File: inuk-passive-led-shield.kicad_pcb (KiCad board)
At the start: 2 copper layers, 90 x 30 mm, 12 parts, among them J1 Conn_01x04_Male, J2 Conn_01x10_Male, J3 Conn_01x02_Male

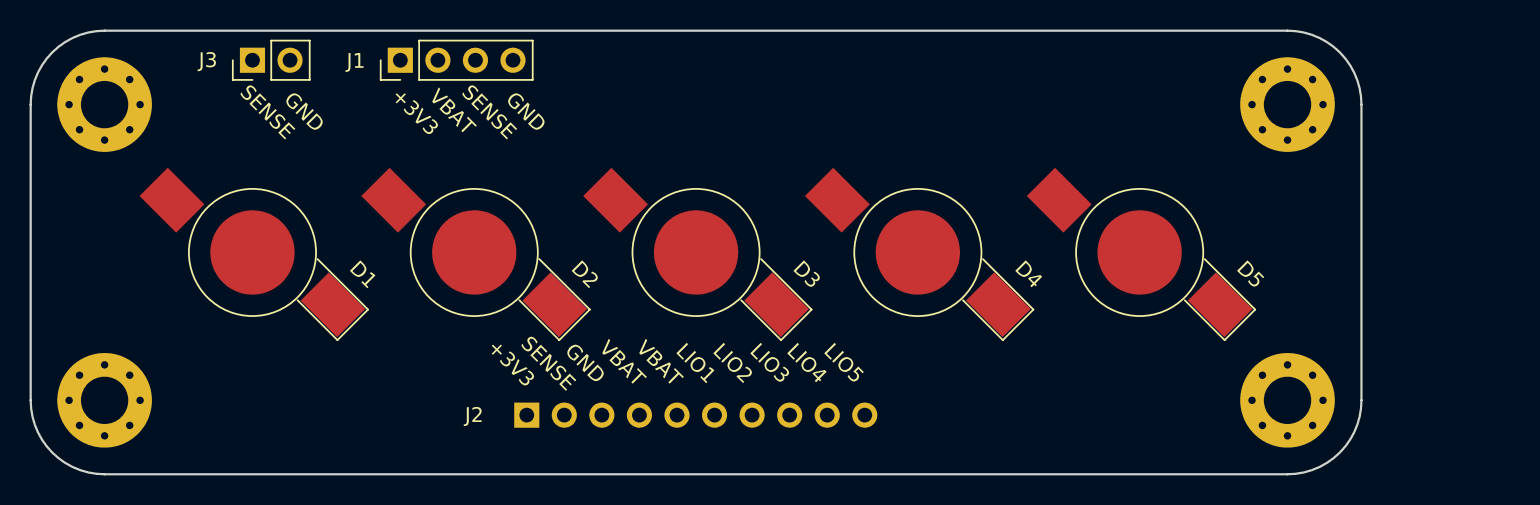
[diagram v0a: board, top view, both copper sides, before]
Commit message: added logo and info text for rev 0.9
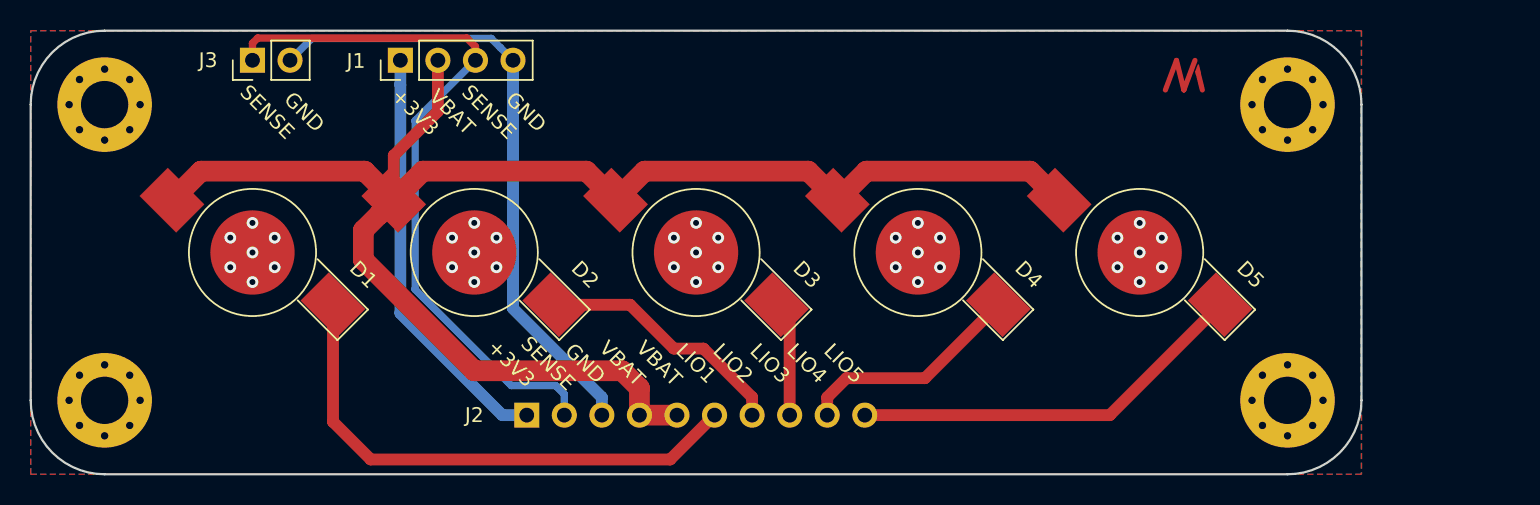
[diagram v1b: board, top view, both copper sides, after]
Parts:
- added U1: Logo_NM, Custom:Logo_NM, F.Cu at (133.0, 118.0)
- D1, D2, D3, D4, D5: value LED -> LED_PAD
- H1, H2, H3, H4: value MountingHole -> MountingHole_Pad
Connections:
- D1 pad 3: (no net) -> /thermal
- D2 pad 3: (no net) -> /thermal
- D3 pad 3: (no net) -> /thermal
- D4 pad 3: (no net) -> /thermal
- D5 pad 3: (no net) -> /thermal
- H1 pad 1: (no net) -> /thermal
- H2 pad 1: (no net) -> /thermal
- H3 pad 1: (no net) -> /thermal
- H4 pad 1: (no net) -> /thermal
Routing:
- net +BATT: track 0.00 -> 108.7 mm
- net /sense: track 0.00 -> 49.2 mm
- net GND: track 0.00 -> 42.8 mm
- net /lio1: track 0.00 -> 36.0 mm
- net +3V3: track 0.00 -> 28.5 mm
- net /lio5: track 0.00 -> 27.1 mm
- net /lio2: track 0.00 -> 17.1 mm
- net /lio4: track 0.00 -> 15.4 mm
- net /lio3: track 0.00 -> 7.83 mm
- net /thermal: vias 0 -> 35
- added copper zone on B.Cu, net /thermal
- added copper zone on F.Cu, net /thermal
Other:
- board text added: "Inuk passive led shield"
- board text added: "Rev: 0.9"

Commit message: resized board to 27 x 100 to fit on 100x100 panel
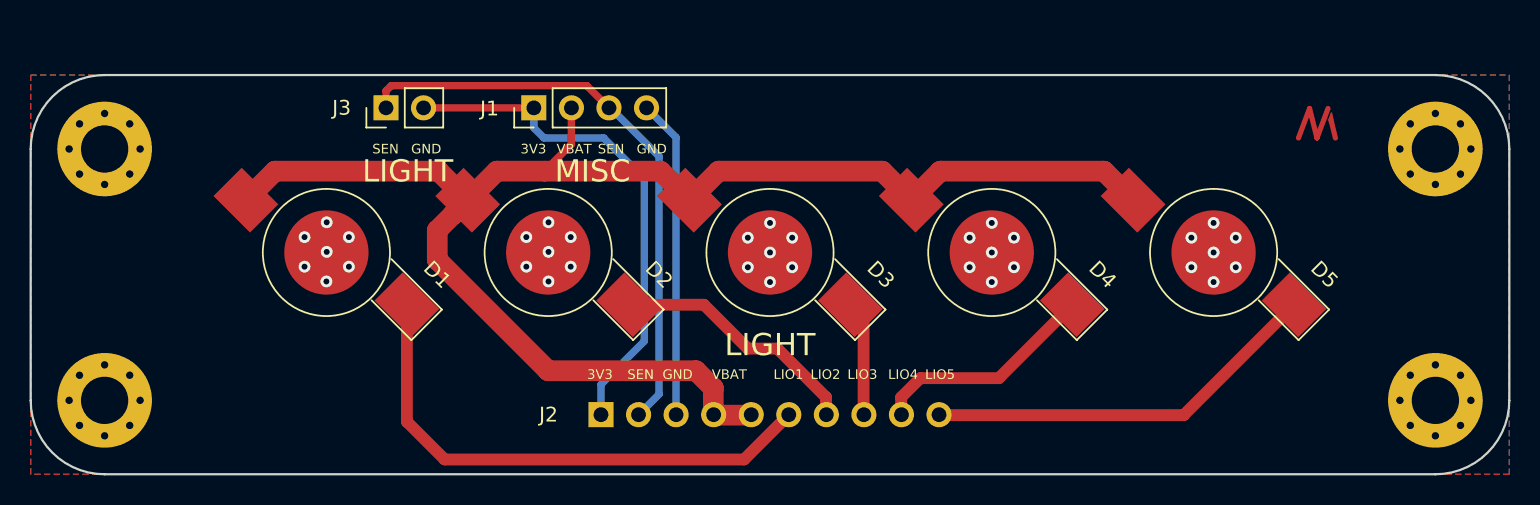
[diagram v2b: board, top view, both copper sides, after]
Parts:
- moved H2 10.4 mm to (150.0, 123.0)
- moved H3 10.0 mm to (150.0, 140.0)
- moved J1 9.59 mm to (89.0, 120.2)
- moved J3 9.59 mm to (79.0, 120.2)
- moved U1 9.57 mm to (142.0, 121.2)
- moved J2 5.02 mm to (93.6, 141.0)
- moved D1 5.00 mm to (75.0, 130.0)
- moved D2 5.00 mm to (90.0, 130.0)
- moved D3 5.00 mm to (105.0, 130.0)
- moved D4 5.00 mm to (120.0, 130.0)
- moved D5 5.00 mm to (135.0, 130.0)
- moved H1 3.00 mm to (60.0, 123.0)
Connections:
- J3 pad 2: GND -> +3V3
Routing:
- net GND: track 42.8 -> 21.6 mm
- net /sense: track 49.2 -> 39.8 mm
- net +3V3: track 28.5 -> 35.4 mm
- net +BATT: track 108.7 -> 103.1 mm
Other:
- board size 90 x 30 mm -> 100 x 27 mm
- board text added: "3V3"
- board text added: "LIGHT"
- board text added: "MISC"
- board text added: "SEN"
- board text removed: "+3V3"
- board text removed: "SENSE"

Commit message: created production files
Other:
- board text added: "Rev: 1.0"
- board text removed: "Rev: 0.9"
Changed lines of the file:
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@@
     (visible_elements FFFFFF7F)
     (pcbplotparams
-      (layerselection 0x00030_ffffffff)
+      (layerselection 0x010ff_ffffffff)
       (usegerberextensions false)
       (usegerberattributes false)
@@
       (drillshape 0)
       (scaleselection 1)
-      (outputdirectory ""))
+      (outputdirectory "production/"))
   )
   (net 0 "")
@@
     )
   )
-  (gr_text LIGHT (at 80.5 124.5) (layer F.SilkS)
+  (gr_text LIGHT (at 80.5 124.4) (layer F.SilkS)
     (effects (font (size 1.5 1.5) (thickness 0.2)))
   )
-  (gr_text MISC (at 93 124.5) (layer F.SilkS)
+  (gr_text MISC (at 93 124.4) (layer F.SilkS)
     (effects (font (size 1.5 1.5) (thickness 0.2)))
   )
-  (gr_text LIGHT (at 105 136.25) (layer F.SilkS)
+  (gr_text LIGHT (at 105 136.6) (layer F.SilkS)
     (effects (font (size 1.5 1.5) (thickness 0.2)))
   )
-  (gr_text SEN (at 79 123) (layer F.SilkS)
-    (effects (font (size 0.65 0.65) (thickness 0.15)))
-  )
-  (gr_text GND (at 81.75 123) (layer F.SilkS)
-    (effects (font (size 0.65 0.65) (thickness 0.15)))
-  )
-  (gr_text GND (at 97 123) (layer F.SilkS)
-    (effects (font (size 0.65 0.65) (thickness 0.15)))
-  )
-  (gr_text SEN (at 94.25 123) (layer F.SilkS)
-    (effects (font (size 0.65 0.65) (thickness 0.15)))
-  )
-  (gr_text VBAT (at 91.75 123) (layer F.SilkS)
-    (effects (font (size 0.65 0.65) (thickness 0.15)))
-  )
-  (gr_text 3V3 (at 89 123) (layer F.SilkS)
-    (effects (font (size 0.65 0.65) (thickness 0.15)))
-  )
-  (gr_text LIO5 (at 116.5 138.25) (layer F.SilkS)
-    (effects (font (size 0.65 0.65) (thickness 0.15)))
-  )
-  (gr_text LIO4 (at 114 138.25) (layer F.SilkS)
-    (effects (font (size 0.65 0.65) (thickness 0.15)))
-  )
-  (gr_text LIO3 (at 111.25 138.25) (layer F.SilkS)
-    (effects (font (size 0.65 0.65) (thickness 0.15)))
-  )
-  (gr_text LIO2 (at 108.75 138.25) (layer F.SilkS)
-    (effects (font (size 0.65 0.65) (thickness 0.15)))
-  )
-  (gr_text LIO1 (at 106.25 138.25) (layer F.SilkS)
-    (effects (font (size 0.65 0.65) (thickness 0.15)))
-  )
-  (gr_text VBAT (at 102.25 138.25) (layer F.SilkS)
-    (effects (font (size 0.65 0.65) (thickness 0.15)))
-  )
-  (gr_text GND (at 98.75 138.25) (layer F.SilkS)
-    (effects (font (size 0.65 0.65) (thickness 0.15)))
-  )
-  (gr_text SEN (at 96.25 138.25) (layer F.SilkS)
-    (effects (font (size 0.65 0.65) (thickness 0.15)))
-  )
-  (gr_text "Rev: 0.9" (at 123.75 121.85) (layer F.Mask)
+  (gr_text SEN (at 79 122.6) (layer F.SilkS)
+    (effects (font (size 0.65 0.65) (thickness 0.15)))
+  )
+  (gr_text GND (at 81.75 122.6) (layer F.SilkS)
+    (effects (font (size 0.65 0.65) (thickness 0.15)))
+  )
+  (gr_text GND (at 97 122.6) (layer F.SilkS)
+    (effects (font (size 0.65 0.65) (thickness 0.15)))
+  )
+  (gr_text SEN (at 94.25 122.6) (layer F.SilkS)
+    (effects (font (size 0.65 0.65) (thickness 0.15)))
+  )
+  (gr_text VBAT (at 91.6 122.6) (layer F.SilkS)
+    (effects (font (size 0.65 0.65) (thickness 0.15)))
+  )
+  (gr_text 3V3 (at 89 122.6) (layer F.SilkS)
+    (effects (font (size 0.65 0.65) (thickness 0.15)))
+  )
+  (gr_text LIO5 (at 116.5 138.55) (layer F.SilkS)
+    (effects (font (size 0.65 0.65) (thickness 0.15)))
+  )
+  (gr_text LIO4 (at 114 138.55) (layer F.SilkS)
+    (effects (font (size 0.65 0.65) (thickness 0.15)))
+  )
+  (gr_text LIO3 (at 111.25 138.55) (layer F.SilkS)
+    (effects (font (size 0.65 0.65) (thickness 0.15)))
+  )
+  (gr_text LIO2 (at 108.75 138.55) (layer F.SilkS)
+    (effects (font (size 0.65 0.65) (thickness 0.15)))
+  )
+  (gr_text LIO1 (at 106.25 138.55) (layer F.SilkS)
+    (effects (font (size 0.65 0.65) (thickness 0.15)))
+  )
+  (gr_text VBAT (at 102.5 138.55) (layer F.SilkS)
+    (effects (font (size 0.65 0.65) (thickness 0.15)))
+  )
+  (gr_text GND (at 98.75 138.55) (layer F.SilkS)
+    (effects (font (size 0.65 0.65) (thickness 0.15)))
+  )
+  (gr_text SEN (at 96.25 138.55) (layer F.SilkS)
+    (effects (font (size 0.65 0.65) (thickness 0.15)))
+  )
+  (gr_text "Rev: 1.0" (at 123.75 121.85) (layer F.Mask)
     (effects (font (size 1 1) (thickness 0.15)))
   )
@@
   (gr_poly (pts (xy 95.5 134.5) (xy 55 134.5) (xy 55 125.5) (xy 95.5 125.5)) (layer B.Mask) (width 0.1))
   (gr_poly (pts (xy 155 134.5) (xy 99.75 134.5) (xy 99.75 125.5) (xy 155 125.5)) (layer B.Mask) (width 0.1))
-  (gr_text 3V3 (at 93.5 138.25) (layer F.SilkS)
-    (effects (font (size 0.65 0.65) (thickness 0.15)))
-  )
+  (gr_text 3V3 (at 93.5 138.55) (layer F.SilkS)
+    (effects (font (size 0.65 0.65) (thickness 0.15)))
+  )
